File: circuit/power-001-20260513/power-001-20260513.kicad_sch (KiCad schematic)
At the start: 34 parts, among them J1 VIN, Q1 NMOS, Q2 PMOS, SW1 SW_SPST, U1 PIC12F683-xSN

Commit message: Update メイン基板の発注ファイルを更新
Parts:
- added C16, C17, C18: 100n, Capacitor_SMD:C_0805_2012Metric, symbol Device:C_Small
- added R16, R17, R18: 10k, Resistor_SMD:R_0805_2012Metric, symbol Device:R_Small
- added SW2, SW3, SW4: SW_SPDT, symbol Switch:SW_SPDT
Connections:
- net +3.3V: now also R16.2, R17.2, R18.2
- net GND: now also C16.2, C17.2, C18.2, SW2.2 (B), SW2.3 (C), SW3.2 (B), SW3.3 (C), SW4.2 (B), SW4.3 (C)
- new net SW_TGL_1: C16.1, R16.1, SW2.1 (A)
- new net SW_TGL_2: C17.1, R17.1, SW3.1 (A)
- new net SW_TGL_3: C18.1, R18.1, SW4.1 (A)

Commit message: Update サブ基板の回路図が完成した
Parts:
- added C8: 100n, Capacitor_SMD:C_0805_2012Metric, symbol Device:C_Small
- added R19, R20: 1k, Resistor_SMD:R_0805_2012Metric, symbol Device:R_Small
- added U5: (no value), symbol @Thrive_symbol_sub:SSD1306
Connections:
- net +3.3V: now also C8.1, R19.1, R20.1, U5.2 (VCC)
- net GND: now also C8.2, U5.1 (GND)
- new net SCL: R20.2, U5.3 (SCL)
- new net SDA: R19.2, U5.4 (SDA)

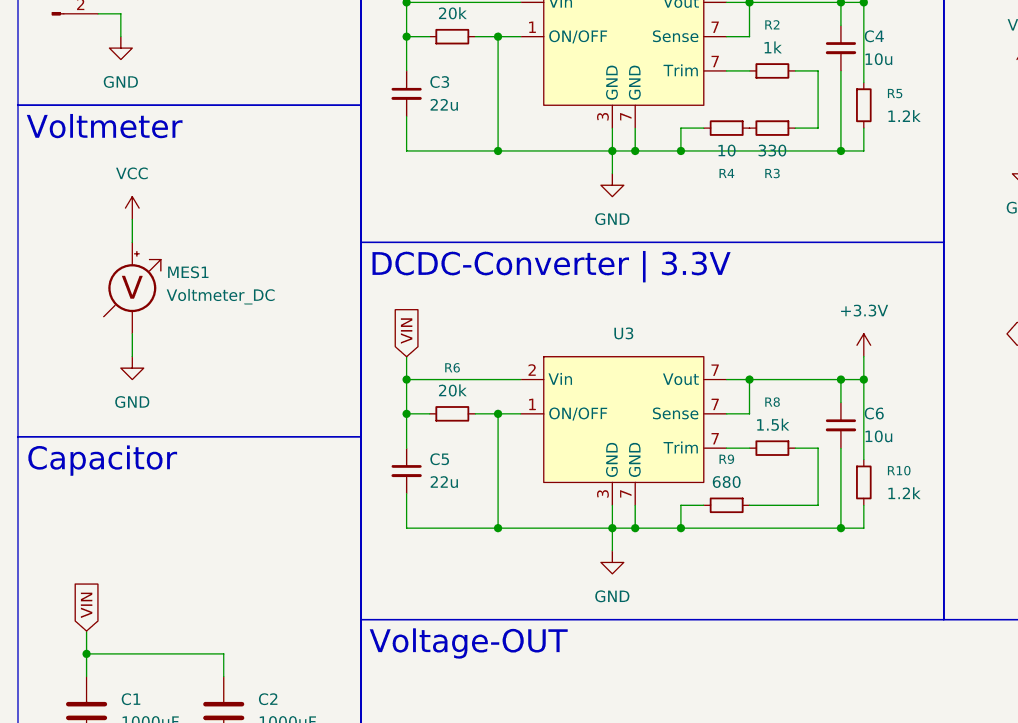
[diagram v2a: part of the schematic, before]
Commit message: Update サブ基板とネオピク基板と電源基板のDXFファイルを更新した
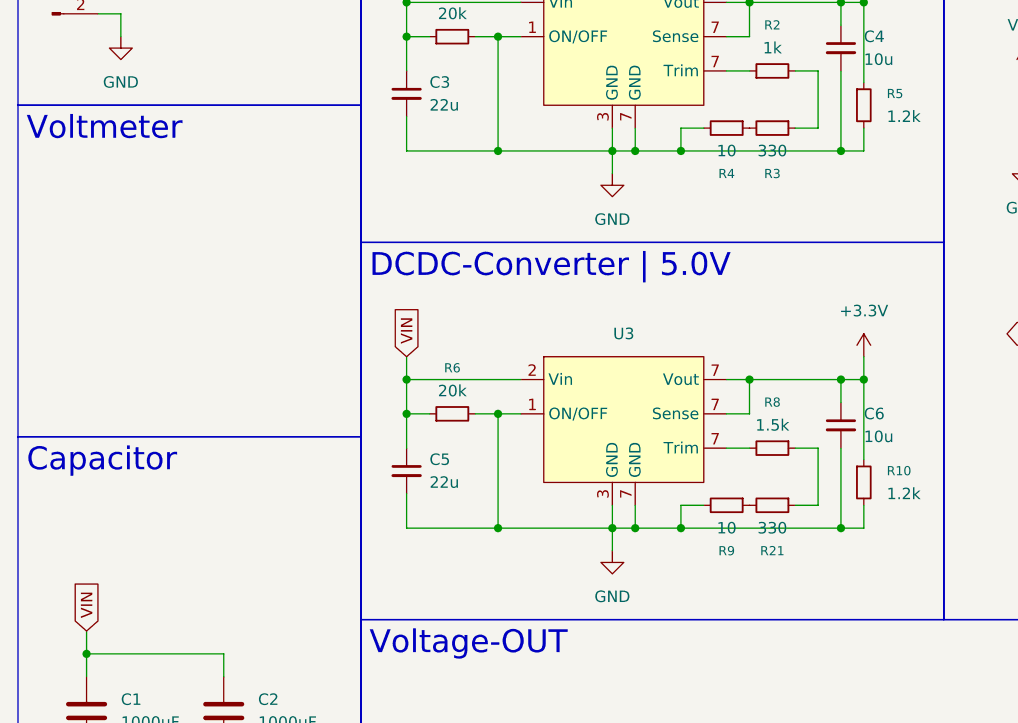
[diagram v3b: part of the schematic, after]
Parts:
- removed MES1: Voltmeter_DC, symbol Device:Voltmeter_DC
- added R21: 330, symbol Device:R_Small
- R9: value 680 -> 10
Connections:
- net at R8.1: now also R21.1; no longer R9.1
- new net: R21.2, R9.1
